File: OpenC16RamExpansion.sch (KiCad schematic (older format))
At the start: 4 parts, among them U1 74LS257, U2 74LS257, U3 4464, U4 4464

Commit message: Complete schematics
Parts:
- added J1: C16-Exp-Port, C16_Cart_Conn:C16_Cart_Conn, symbol C16-Exp-Port
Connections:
- net GND: now also J1.1 (GND), J1.25 (GND), J1.A (GND), J1.CC (GND)
- net VCC: now also J1.2 (VCC), J1.3 (VCC)
- net c16_a0: now also J1.Y (A0)
- net c16_a1: now also J1.X (A1)
- net c16_a10: now also J1.M (A10)
- net c16_a11: now also J1.L (A11)
- net c16_a12: now also J1.K (A12)
- net c16_a13: now also J1.J (A13)
- net c16_a14: now also J1.H (A14)
- net c16_a15: now also J1.F (A15)
- net c16_a2: now also J1.W (A2)
- net c16_a3: now also J1.V (A3)
- net c16_a4: now also J1.U (A4)
- net c16_a5: now also J1.T (A5)
- net c16_a6: now also J1.S (A6)
- net c16_a7: now also J1.R (A7)
- net c16_a8: now also J1.P (A8)
- net c16_a9: now also J1.N (A9)
- net d0: now also J1.21 (D0)
- net d1: now also J1.20 (D1)
- net d2: now also J1.19 (D2)
- net d3: now also J1.18 (D3)
- net d4: now also J1.17 (D4)
- net d5: now also J1.16 (D5)
- net d6: now also J1.15 (D6)
- net d7: now also J1.14 (D7)
- net sel: now reaches U1.1 (S), U2.1 (S)
- net sel: now also J1.12 (MUX)
- net /cas: now reaches U3.16 (CAS), U4.16 (CAS)
- net /cas: now also J1.11 (/CAS)
- net r/w: now reaches U3.4 (R/W), U4.4 (R/W)
- net r/w: now also J1.5 (R/W)
- net /ras: now reaches U3.5 (RAS), U4.5 (RAS)
- net /ras: now also J1.D (/RAS)
- no-connect marks 0 -> 13
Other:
- moved on the sheet: U1, U2, U3, U4

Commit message: Almost there...
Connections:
- net a0 is gone; now on net /cas: U1.4 (Y1), U3.14 (A0), U4.14 (A0)
- net a1 is gone; now on net /cas: U1.7 (Y2), U3.13 (A1), U4.13 (A1)
- net a2 is gone; now on net /cas: U1.9 (Y3), U3.12 (A2), U4.12 (A2)
- net a3 is gone; now on net /cas: U1.12 (Y4), U3.11 (A3), U4.11 (A3)
- net a7 is gone; now on net /cas: U2.12 (Y4), U3.10 (A7), U4.10 (A7)
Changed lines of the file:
@@
 L GND #PWR06
 U 1 1 598EC57B
-P 10750 1050
-F 0 "#PWR06" H 10750 800 50  0001 C CNN
-F 1 "GND" H 10750 900 50  0000 C CNN
-F 2 "" H 10750 1050 50  0001 C CNN
-F 3 "" H 10750 1050 50  0001 C CNN
-	1    10750 1050
+P 10750 1100
+F 0 "#PWR06" H 10750 850 50  0001 C CNN
+F 1 "GND" H 10750 950 50  0000 C CNN
+F 2 "" H 10750 1100 50  0001 C CNN
+F 3 "" H 10750 1100 50  0001 C CNN
+	1    10750 1100
 	1    0    0    -1
 $EndComp
@@
 L PWR_FLAG #FLG07
 U 1 1 598EC590
-P 10750 850
-F 0 "#FLG07" H 10750 925 50  0001 C CNN
-F 1 "PWR_FLAG" H 10750 1000 50  0000 C CNN
-F 2 "" H 10750 850 50  0001 C CNN
-F 3 "" H 10750 850 50  0001 C CNN
-	1    10750 850
+P 10750 900
+F 0 "#FLG07" H 10750 975 50  0001 C CNN
+F 1 "PWR_FLAG" H 10750 1100 50  0000 C CNN
+F 2 "" H 10750 900 50  0001 C CNN
+F 3 "" H 10750 900 50  0001 C CNN
+	1    10750 900
 	1    0    0    -1
 $EndComp
@@
 P 10300 1050
 F 0 "#FLG08" H 10300 1125 50  0001 C CNN
-F 1 "PWR_FLAG" H 10300 1200 50  0000 C CNN
+F 1 "PWR_FLAG" H 10300 1250 50  0000 C CNN
 F 2 "" H 10300 1050 50  0001 C CNN
 F 3 "" H 10300 1050 50  0001 C CNN
@@
 NoConn ~ 10150 4350
 Wire Wire Line
-	6200 2150 7050 2150
+	6200 2150 6450 2150
+Wire Wire Line
+	6450 2150 7050 2150
 Wire Wire Line
 	7050 2150 7050 2300
@@
 	7050 3850 7050 3950
 Wire Wire Line
-	6200 3850 7050 3850
+	6200 3850 6300 3850
+Wire Wire Line
+	6300 3850 7050 3850
 Wire Wire Line
 	4850 4950 4650 4950
@@
 	10300 850  10300 1050
 Wire Wire Line
-	10750 1050 10750 850
+	10750 1100 10750 900
 Wire Wire Line
 	6550 4050 6200 4050
 Wire Wire Line
-	6550 1550 6550 4050
+	6550 1550 6550 2350
+Wire Wire Line
+	6550 2350 6550 2550
+Wire Wire Line
+	6550 2550 6550 2650
+Wire Wire Line
+	6550 2650 6550 2750
+Wire Wire Line
+	6550 2750 6550 2850
+Wire Wire Line
+	6550 2850 6550 2950
+Wire Wire Line
+	6550 2950 6550 4050
 Wire Wire Line
 	6550 2350 6200 2350
@@
 	6200 4650 6550 4650
 Wire Bus Line
-	6650 2650 6650 5350
+	6650 2650 6650 2750
+Wire Bus Line
+	6650 2750 6650 2850
+Wire Bus Line
+	6650 2850 6650 2950
+Wire Bus Line
+	6650 2950 6650 3050
+Wire Bus Line
+	6650 3050 6650 4350
+Wire Bus Line
+	6650 4350 6650 4450
+Wire Bus Line
+	6650 4450 6650 4550
+Wire Bus Line
+	6650 4550 6650 4650
+Wire Bus Line
+	6650 4650 6650 4750
+Wire Bus Line
+	6650 4750 6650 5350
 Wire Wire Line
 	4400 4250 4700 4250
 Wire Wire Line
-	4400 1450 4400 4250
+	4400 1450 4400 2550
+Wire Wire Line
+	4400 2550 4400 4250
 Wire Wire Line
 	4400 2550 4700 2550
@@
 	4700 4550 4350 4550
 Wire Bus Line
-	4250 2550 4250 5350
+	4250 2550 4250 2650
+Wire Bus Line
+	4250 2650 4250 2750
+Wire Bus Line
+	4250 2750 4250 4250
+Wire Bus Line
+	4250 4250 4250 4350
+Wire Bus Line
+	4250 4350 4250 4450
+Wire Bus Line
+	4250 4450 4250 5350
 Wire Wire Line
 	1500 3100 1250 3100
@@
 	1500 3000 700  3000
 Wire Wire Line
-	700  1650 700  4700
+	700  1650 700  3000
+Wire Wire Line
+	700  3000 700  4700
 Wire Wire Line
 	700  4700 1500 4700
@@
 	6200 4150 6750 4150
 Wire Bus Line
-	6850 2350 6850 5500
+	6850 2350 6850 2550
+Wire Bus Line
+	6850 2550 6850 4050
+Wire Bus Line
+	6850 4050 6850 4250
+Wire Bus Line
+	6850 4250 6850 5500
 Wire Bus Line
 	10650 5500 4050 5500
@@
 	4700 4050 4150 4050
 Wire Bus Line
-	4050 5500 4050 2150
+	4050 5500 4050 3950
+Wire Bus Line
+	4050 3950 4050 3850
+Wire Bus Line
+	4050 3850 4050 2250
+Wire Bus Line
+	4050 2250 4050 2150
 Wire Wire Line
 	4500 4150 4700 4150
 Wire Wire Line
-	4500 1750 4500 4150
+	4500 1750 4500 2450
+Wire Wire Line
+	4500 2450 4500 4150
 Wire Wire Line
 	4500 2450 4700 2450
@@
 	1500 4550 900  4550
 Wire Bus Line
-	800  1900 800  5650
+	800  1900 800  2000
+Wire Bus Line
+	800  2000 800  2150
+Wire Bus Line
+	800  2150 800  2250
+Wire Bus Line
+	800  2250 800  2400
+Wire Bus Line
+	800  2400 800  2500
+Wire Bus Line
+	800  2500 800  2650
+Wire Bus Line
+	800  2650 800  2750
+Wire Bus Line
+	800  2750 800  3600
+Wire Bus Line
+	800  3600 800  3700
+Wire Bus Line
+	800  3700 800  3850
+Wire Bus Line
+	800  3850 800  3950
+Wire Bus Line
+	800  3950 800  4100
+Wire Bus Line
+	800  4100 800  4200
+Wire Bus Line
+	800  4200 800  4350
+Wire Bus Line
+	800  4350 800  4450
+Wire Bus Line
+	800  4450 800  5650
 Wire Wire Line
 	3000 2050 3450 2050
@@
 	3000 4500 3450 4500
 Wire Bus Line
-	3550 2150 3550 5350
+	3550 2150 3550 2400
+Wire Bus Line
+	3550 2400 3550 2650
+Wire Bus Line
+	3550 2650 3550 2900
+Wire Bus Line
+	3550 2900 3550 3850
+Wire Bus Line
+	3550 3850 3550 4100
+Wire Bus Line
+	3550 4100 3550 4350
+Wire Bus Line
+	3550 4350 3550 4600
+Wire Bus Line
+	3550 4600 3550 5350
 Wire Wire Line
 	8650 2650 8300 2650
@@
 	8650 4150 8300 4150
 Wire Bus Line
-	8200 2550 8200 5650
+	8200 2550 8200 2650
+Wire Bus Line
+	8200 2650 8200 2750
+Wire Bus Line
+	8200 2750 8200 2850
+Wire Bus Line
+	8200 2850 8200 2950
+Wire Bus Line
+	8200 2950 8200 3050
+Wire Bus Line
+	8200 3050 8200 3150
+Wire Bus Line
+	8200 3150 8200 3250
+Wire Bus Line
+	8200 3250 8200 3350
+Wire Bus Line
+	8200 3350 8200 3450
+Wire Bus Line
+	8200 3450 8200 3550
+Wire Bus Line
+	8200 3550 8200 3650
+Wire Bus Line
+	8200 3650 8200 3750
+Wire Bus Line
+	8200 3750 8200 3850
+Wire Bus Line
+	8200 3850 8200 3950
+Wire Bus Line
+	8200 3950 8200 4050
+Wire Bus Line
+	8200 4050 8200 5650
 Wire Wire Line
 	8650 2250 8300 2250
@@
 	10450 1850 10450 2250
 Wire Wire Line
-	10150 2250 10650 2250
+	10150 2250 10450 2250
+Wire Wire Line
+	10450 2250 10650 2250
 Connection ~ 10450 2250
 Wire Wire Line
@@
 	8550 4650 8550 5000
 Wire Wire Line
-	8550 5000 10400 5000
+	8550 5000 10250 5000
+Wire Wire Line
+	10250 5000 10400 5000
 Wire Wire Line
 	10250 5000 10250 4650
@@
 	10150 3350 10550 3350
 Wire Bus Line
-	10650 2750 10650 5500
+	10650 2750 10650 2850
+Wire Bus Line
+	10650 2850 10650 2950
+Wire Bus Line
+	10650 2950 10650 3050
+Wire Bus Line
+	10650 3050 10650 3150
+Wire Bus Line
+	10650 3150 10650 3250
+Wire Bus Line
+	10650 3250 10650 3350
+Wire Bus Line
+	10650 3350 10650 3450
+Wire Bus Line
+	10650 3450 10650 5500
 Wire Bus Line
 	3550 5350 6650 5350
@@
 $EndComp
 Wire Wire Line
-	10150 4450 10400 4450
+	10150 4450 10250 4450
+Wire Wire Line
+	10250 4450 10400 4450
 Wire Wire Line
 	10150 4550 10250 4550

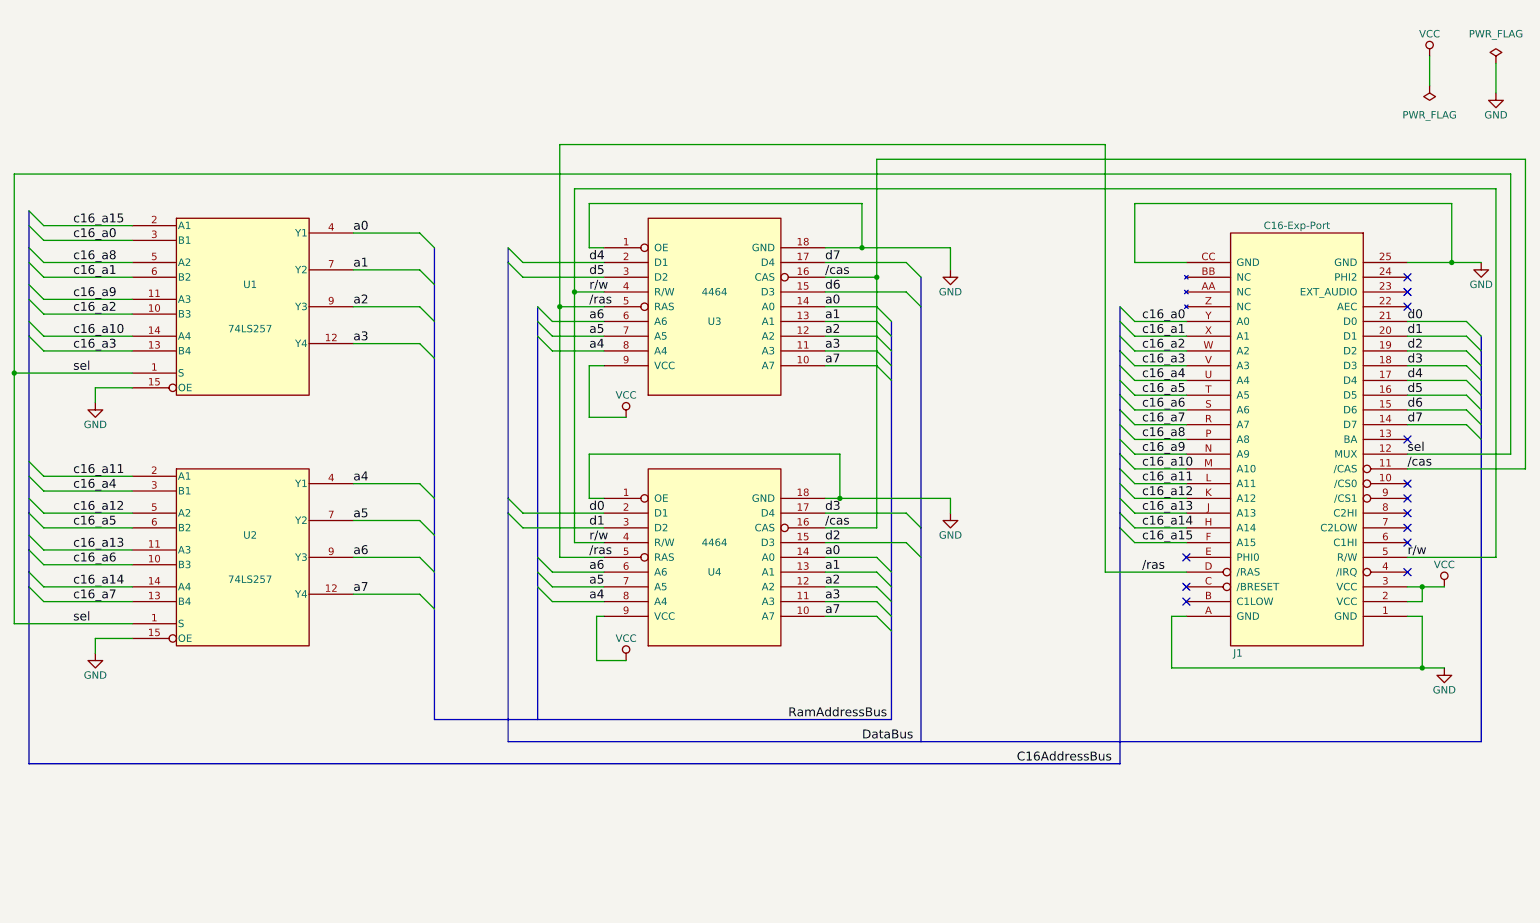
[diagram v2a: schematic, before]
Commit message: Add decoupling caps
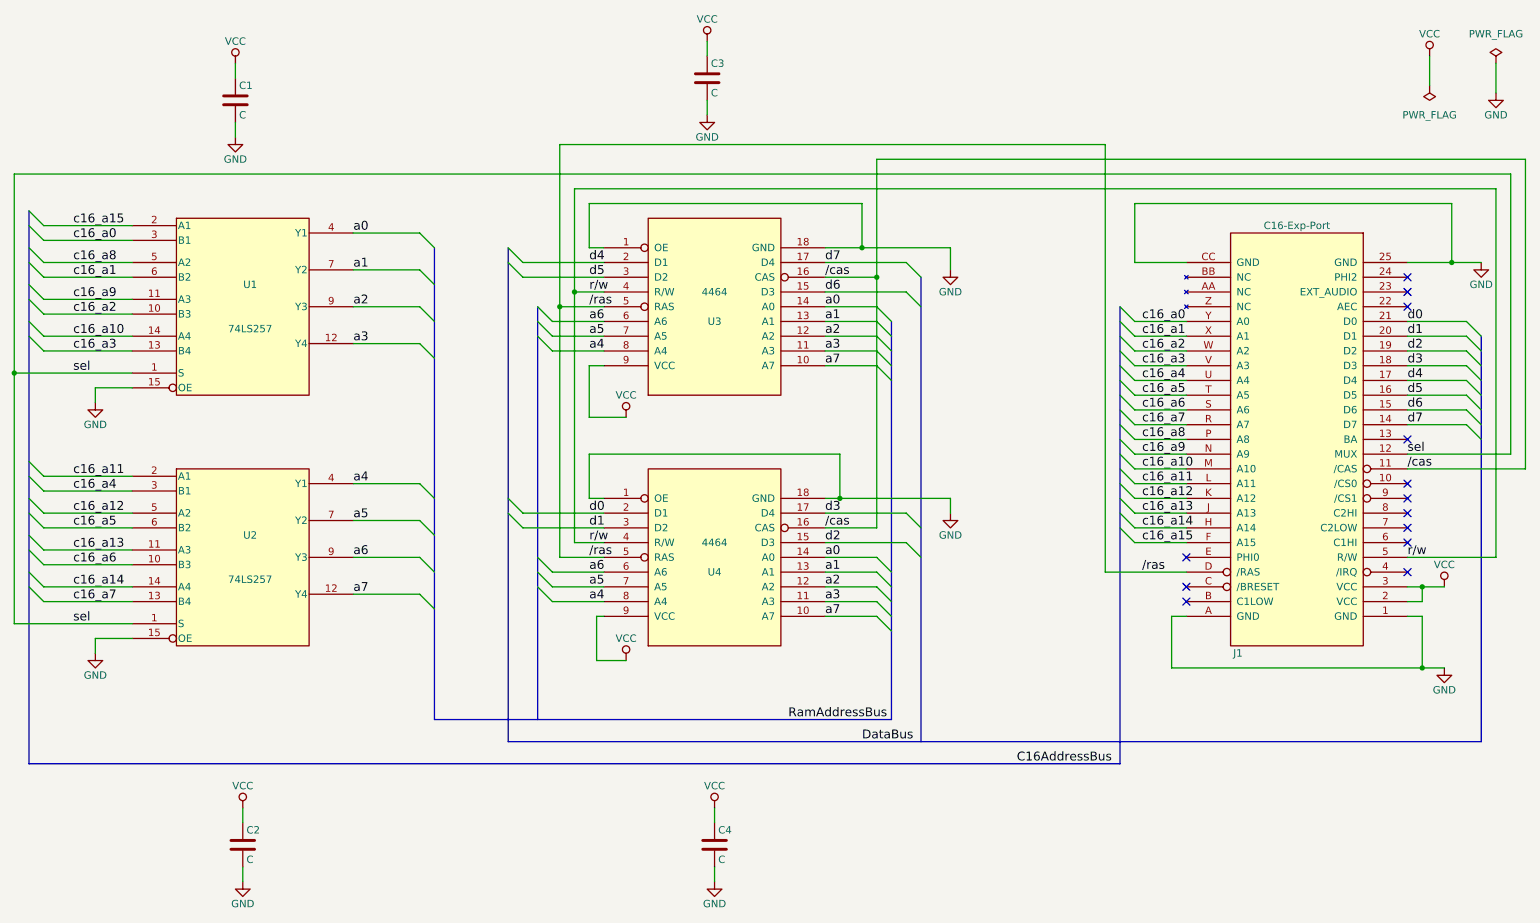
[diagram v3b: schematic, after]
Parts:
- added C1, C2, C3, C4: C, Capacitors_SMD:C_0805_HandSoldering, symbol C
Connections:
- net /cas: no longer U1.12 (Y4), U1.4 (Y1), U1.7 (Y2), U1.9 (Y3), U2.12 (Y4), U3.10 (A7), U3.11 (A3), U3.12 (A2), U3.13 (A1), U3.14 (A0), U4.10 (A7), U4.11 (A3), U4.12 (A2), U4.13 (A1), U4.14 (A0)
- net GND: now also C1.2, C2.2, C3.2, C4.2
- net VCC: now also C1.1, C2.1, C3.1, C4.1
- new net a0: U1.4 (Y1), U3.14 (A0), U4.14 (A0)
- new net a1: U1.7 (Y2), U3.13 (A1), U4.13 (A1)
- new net a2: U1.9 (Y3), U3.12 (A2), U4.12 (A2)
- new net a3: U1.12 (Y4), U3.11 (A3), U4.11 (A3)
- new net a7: U2.12 (Y4), U3.10 (A7), U4.10 (A7)

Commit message: Space edge connector pins 2.0mm apart, improve ground plane and some other tweaks
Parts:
- J1: footprint C16_Cart_Conn:C16_Cart_Conn -> OpenC16RamExpansion:C16_Cart_Conn
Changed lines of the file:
@@
 Sheet 1 1
 Title "Open Commodore 16 64 kB RAM Expansion"
-Date "2017-08-21"
-Rev "1.0"
+Date "2018-01-01"
+Rev "2"
 Comp "SukkoPera"
 Comment1 ""
@@
 $EndComp
 $Comp
-L GND #PWR13
+L GND #PWR01
 U 1 1 598EC4C1
 P 7050 2300
-F 0 "#PWR13" H 7050 2050 50  0001 C CNN
+F 0 "#PWR01" H 7050 2050 50  0001 C CNN
 F 1 "GND" H 7050 2150 50  0000 C CNN
 F 2 "" H 7050 2300 50  0001 C CNN
@@
 $EndComp
 $Comp
-L GND #PWR14
+L GND #PWR02
 U 1 1 598EC4E5
 P 7050 3950
-F 0 "#PWR14" H 7050 3700 50  0001 C CNN
+F 0 "#PWR02" H 7050 3700 50  0001 C CNN
 F 1 "GND" H 7050 3800 50  0000 C CNN
 F 2 "" H 7050 3950 50  0001 C CNN
@@
 $EndComp
 $Comp
-L VCC #PWR8
+L VCC #PWR03
 U 1 1 598EC502
 P 4850 4950
-F 0 "#PWR8" H 4850 4800 50  0001 C CNN
+F 0 "#PWR03" H 4850 4800 50  0001 C CNN
 F 1 "VCC" H 4850 5100 50  0000 C CNN
 F 2 "" H 4850 4950 50  0001 C CNN
@@
 $EndComp
 $Comp
-L VCC #PWR7
+L VCC #PWR04
 U 1 1 598EC52F
 P 4850 3300
-F 0 "#PWR7" H 4850 3150 50  0001 C CNN
+F 0 "#PWR04" H 4850 3150 50  0001 C CNN
 F 1 "VCC" H 4850 3450 50  0000 C CNN
 F 2 "" H 4850 3300 50  0001 C CNN
@@
 $EndComp
 $Comp
-L VCC #PWR15
+L VCC #PWR05
 U 1 1 598EC558
 P 10300 850
-F 0 "#PWR15" H 10300 700 50  0001 C CNN
+F 0 "#PWR05" H 10300 700 50  0001 C CNN
 F 1 "VCC" H 10300 1000 50  0000 C CNN
 F 2 "" H 10300 850 50  0001 C CNN
@@
 $EndComp
 $Comp
-L GND #PWR19
+L GND #PWR06
 U 1 1 598EC57B
 P 10750 1100
-F 0 "#PWR19" H 10750 850 50  0001 C CNN
+F 0 "#PWR06" H 10750 850 50  0001 C CNN
 F 1 "GND" H 10750 950 50  0000 C CNN
 F 2 "" H 10750 1100 50  0001 C CNN
@@
 $EndComp
 $Comp
-L PWR_FLAG #FLG2
+L PWR_FLAG #FLG07
 U 1 1 598EC590
 P 10750 900
-F 0 "#FLG2" H 10750 975 50  0001 C CNN
+F 0 "#FLG07" H 10750 975 50  0001 C CNN
 F 1 "PWR_FLAG" H 10750 1100 50  0000 C CNN
 F 2 "" H 10750 900 50  0001 C CNN
@@
 $EndComp
 $Comp
-L PWR_FLAG #FLG1
+L PWR_FLAG #FLG08
 U 1 1 598EC5C2
 P 10300 1050
-F 0 "#FLG1" H 10300 1125 50  0001 C CNN
+F 0 "#FLG08" H 10300 1125 50  0001 C CNN
 F 1 "PWR_FLAG" H 10300 1250 50  0000 C CNN
 F 2 "" H 10300 1050 50  0001 C CNN
@@
 a4
 $Comp
-L GND #PWR1
+L GND #PWR09
 U 1 1 598ECB65
 P 1250 3200
-F 0 "#PWR1" H 1250 2950 50  0001 C CNN
+F 0 "#PWR09" H 1250 2950 50  0001 C CNN
 F 1 "GND" H 1250 3050 50  0000 C CNN
 F 2 "" H 1250 3200 50  0001 C CNN
@@
 $EndComp
 $Comp
-L GND #PWR2
+L GND #PWR010
 U 1 1 598ECB80
 P 1250 4900
-F 0 "#PWR2" H 1250 4650 50  0001 C CNN
+F 0 "#PWR010" H 1250 4650 50  0001 C CNN
 F 1 "GND" H 1250 4750 50  0000 C CNN
 F 2 "" H 1250 4900 50  0001 C CNN
@@
 F 0 "J1" H 9800 4900 50  0000 C CNN
 F 1 "C16-Exp-Port" H 9400 2000 50  0000 C CNN
-F 2 "C16_Cart_Conn:C16_Cart_Conn" H 9400 1800 50  0001 C CNN
+F 2 "OpenC16RamExpansion:C16_Cart_Conn" H 9400 1800 50  0001 C CNN
 F 3 "DOCUMENTATION" H 9400 1700 50  0001 C CNN
 	1    9400 3450
@@
 	8200 4050 8300 4150
 $Comp
-L GND #PWR18
+L GND #PWR011
 U 1 1 599A17B3
 P 10650 2250
-F 0 "#PWR18" H 10650 2000 50  0001 C CNN
+F 0 "#PWR011" H 10650 2000 50  0001 C CNN
 F 1 "GND" H 10650 2100 50  0000 C CNN
 F 2 "" H 10650 2250 50  0001 C CNN
@@
 $EndComp
 $Comp
-L GND #PWR17
+L GND #PWR012
 U 1 1 599A1913
 P 10400 5000
-F 0 "#PWR17" H 10400 4750 50  0001 C CNN
+F 0 "#PWR012" H 10400 4750 50  0001 C CNN
 F 1 "GND" H 10400 4850 50  0000 C CNN
 F 2 "" H 10400 5000 50  0001 C CNN
@@
 C16AddressBus
 $Comp
-L VCC #PWR16
+L VCC #PWR013
 U 1 1 599A28E4
 P 10400 4450
-F 0 "#PWR16" H 10400 4300 50  0001 C CNN
+F 0 "#PWR013" H 10400 4300 50  0001 C CNN
 F 1 "VCC" H 10400 4600 50  0000 C CNN
 F 2 "" H 10400 4450 50  0001 C CNN
@@
 	2200 1000 2200 900
 $Comp
-L VCC #PWR3
+L VCC #PWR014
 U 1 1 59AAE2CC
 P 2200 900
-F 0 "#PWR3" H 2200 750 50  0001 C CNN
+F 0 "#PWR014" H 2200 750 50  0001 C CNN
 F 1 "VCC" H 2200 1050 50  0000 C CNN
 F 2 "" H 2200 900 50  0001 C CNN
@@
 $EndComp
 $Comp
-L GND #PWR4
+L GND #PWR015
 U 1 1 59AAE32B
 P 2200 1400
-F 0 "#PWR4" H 2200 1150 50  0001 C CNN
+F 0 "#PWR015" H 2200 1150 50  0001 C CNN
 F 1 "GND" H 2200 1250 50  0000 C CNN
 F 2 "" H 2200 1400 50  0001 C CNN
@@
 	5400 850  5400 750
 $Comp
-L VCC #PWR9
+L VCC #PWR016
 U 1 1 59AAE416
 P 5400 750
-F 0 "#PWR9" H 5400 600 50  0001 C CNN
+F 0 "#PWR016" H 5400 600 50  0001 C CNN
 F 1 "VCC" H 5400 900 50  0000 C CNN
 F 2 "" H 5400 750 50  0001 C CNN
@@
 $EndComp
 $Comp
-L GND #PWR10
+L GND #PWR017
 U 1 1 59AAE41C
 P 5400 1250
-F 0 "#PWR10" H 5400 1000 50  0001 C CNN
+F 0 "#PWR017" H 5400 1000 50  0001 C CNN
 F 1 "GND" H 5400 1100 50  0000 C CNN
 F 2 "" H 5400 1250 50  0001 C CNN
@@
 	2250 6050 2250 5950
 $Comp
-L VCC #PWR5
+L VCC #PWR018
 U 1 1 59AAE584
 P 2250 5950
-F 0 "#PWR5" H 2250 5800 50  0001 C CNN
+F 0 "#PWR018" H 2250 5800 50  0001 C CNN
 F 1 "VCC" H 2250 6100 50  0000 C CNN
 F 2 "" H 2250 5950 50  0001 C CNN
@@
 $EndComp
 $Comp
-L GND #PWR6
+L GND #PWR019
 U 1 1 59AAE58A
 P 2250 6450
-F 0 "#PWR6" H 2250 6200 50  0001 C CNN
+F 0 "#PWR019" H 2250 6200 50  0001 C CNN
 F 1 "GND" H 2250 6300 50  0000 C CNN
 F 2 "" H 2250 6450 50  0001 C CNN
@@
 	5450 6050 5450 5950
 $Comp
-L VCC #PWR11
+L VCC #PWR020
 U 1 1 59AAE6A8
 P 5450 5950
-F 0 "#PWR11" H 5450 5800 50  0001 C CNN
+F 0 "#PWR020" H 5450 5800 50  0001 C CNN
 F 1 "VCC" H 5450 6100 50  0000 C CNN
 F 2 "" H 5450 5950 50  0001 C CNN
@@
 $EndComp
 $Comp
-L GND #PWR12
+L GND #PWR021
 U 1 1 59AAE6AE
 P 5450 6450
-F 0 "#PWR12" H 5450 6200 50  0001 C CNN
+F 0 "#PWR021" H 5450 6200 50  0001 C CNN
 F 1 "GND" H 5450 6300 50  0000 C CNN
 F 2 "" H 5450 6450 50  0001 C CNN
